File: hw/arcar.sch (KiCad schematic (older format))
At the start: 30 parts

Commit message: updated schematic, change microcontoler to ATmega328PB and added H bridge, MPU-6050, USB to UART converter and power source
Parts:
- removed C?: 1000u/50V, symbol CP
- removed D?: D, symbol D
- removed D?: D_Bridge_+-AA, symbol D_Bridge_+-AA
- removed J?: POWER, symbol Conn_01x02
- removed M? (x2): Motor_DC, symbol Motor_DC
- removed Q?: Q_NMOS_DGS, symbol Q_NMOS_DGS
- removed R?: 1k, symbol R
- removed U?: ATMEGA328P-AU, Housings_QFP:TQFP-32_7x7mm_Pitch0.8mm, symbol ATMEGA328P-AU
- added C1, C11, C2, C3, C4, C5, C6, C7: 100n, symbol C
- added C12: 2n2, symbol C
- added C13: 4700u/50V, symbol CP
- added C14: 470n, symbol C
- added C8: 10n, symbol C
- added J1: USB_B_Micro, Connectors:USB_Micro-B_10103594-0001LF, symbol USB_B_Micro
- added J2: HEADER, symbol Conn_01x10
- added J3: MOTOR, symbol Conn_01x02
- added R1: 10k, symbol R
- added R3, R4: 4k7, symbol R
- added U1: USBLC6-2SC6, TO_SOT_Packages_SMD:SOT-23-6, symbol USBLC6-2SC6
- added U2: ATMEGA328PB-AU, Housings_QFP:TQFP-32_7x7mm_Pitch0.8mm, symbol ATMEGA328PB-AU
- added U3: CP2102, Housings_DFN_QFN:QFN-28-1EP_5x5mm_Pitch0.5mm, symbol CP2102
- added U4: MPU-6050, symbol MPU-6050
- added U6: TLE52062GAUMA1, TO_SOT_Packages_SMD:TO-263-7_TabPin4, symbol TLE52062GAUMA1
- gave numbers to parts that had none: 21
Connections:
- net labels added: +5V, MOTOR_ERR, MOTOR_PWM1, MOTOR_PWM2, MPU-6050-INT, PD4, PD5, PD6, PD7, PE0, PE1, PE2, PE3
- net labels removed: MOTOR
- wire segments 85 -> 162
- no-connect marks 19 -> 23
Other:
- note removed: "BLOKOVÁNÍ"
- note removed: "ZDROJ"
- note removed: "zatím neznámích parametrů"
- note removed: "← MOŽNOSTI ↓"
- moved on the sheet: C10, C9, D1, D2, D3, D4, D5, P1, R2, R5, R6, R7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

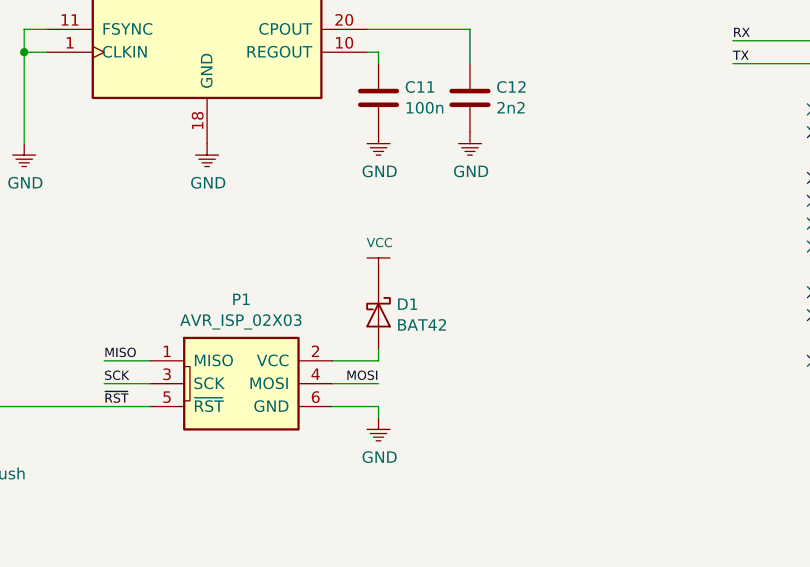
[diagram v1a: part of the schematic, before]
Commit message: updated schematic, chnde ISP VCC conection before LDO
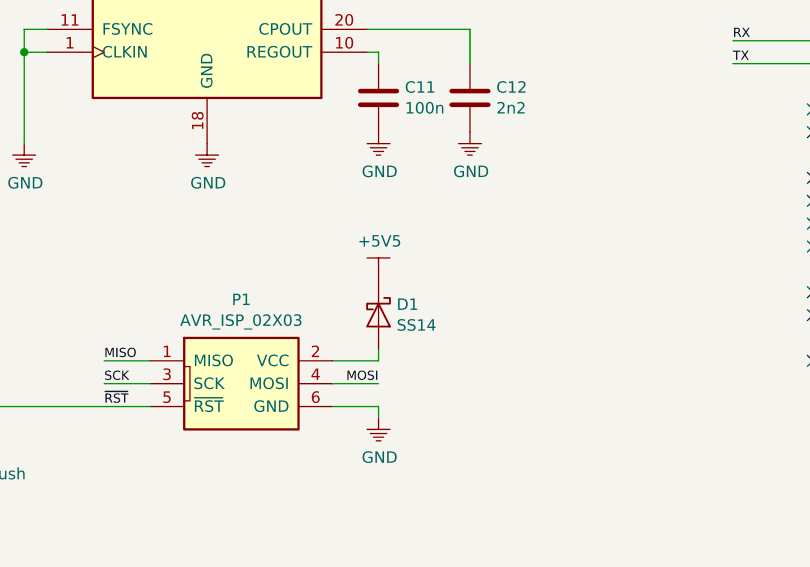
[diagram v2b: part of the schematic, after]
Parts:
- D1: value BAT42 -> SS14
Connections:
- net VCC: no longer D1.1 (K)
- new net +5V5: D1.1 (K)
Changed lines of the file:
@@
 P 7550 5600
 F 0 "D1" V 7504 5679 50  0000 L CNN
-F 1 "BAT42" V 7595 5679 50  0000 L CNN
+F 1 "SS14" V 7595 5679 50  0000 L CNN
 F 2 "" H 7550 5600 50  0001 C CNN
 F 3 "" H 7550 5600 50  0001 C CNN
 	1    7550 5600
 	0    1    1    0
-$EndComp
-$Comp
-L VCC #PWR021
-U 1 1 59F5914F
-P 7550 5450
-F 0 "#PWR021" H 7550 5300 50  0001 C CNN
-F 1 "VCC" H 7555 5616 40  0000 C CNN
-F 2 "" H 7550 5450 50  0001 C CNN
-F 3 "" H 7550 5450 50  0001 C CNN
-	1    7550 5450
-	1    0    0    -1
 $EndComp
 Text Label 9100 4200 0    40   ~ 0
@@
 Text Label 9900 1600 0    40   ~ 0
 PE3
+$Comp
+L +5V5 #PWR?
+U 1 1 59FB343D
+P 7550 5450
+F 0 "#PWR?" H 7550 5150 50  0001 C CNN
+F 1 "+5V5" H 7555 5623 50  0000 C CNN
+F 2 "" H 7550 5450 50  0001 C CNN
+F 3 "" H 7550 5450 50  0001 C CNN
+	1    7550 5450
+	1    0    0    -1
+$EndComp
 $EndSCHEMATC

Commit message: updated schematic
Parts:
- removed J2: HEADER, symbol Conn_01x10
- removed M1: screw, symbol screw
- removed U4: MPU-6050, symbol MPU-6050
- removed Y1: 8MHz, symbol Crystal
- added AFF1: LTS-6960HR, Displays_7-Segment:LTS-69xx, symbol LTS-6960HR
- added C13: 100n, symbol C
- added C14: 10u, symbol C
- added J2: GPIO, symbol Conn_01x04
- added R10, R11, R12, R6, R7, R8, R9: 330R, symbol R
- added R13, R5: 10k, symbol R
- added U4: ULN2003A, symbol ULN2003A
- added U5: LSM9DS1, Housings_LGA:LGA-24L_3x3.5mm_Pitch0.43mm, symbol LSM9DS1
- C10: value 18p -> 100n
- C12: value 2n2 -> 100n
- C9: value 18p -> 10n
- D1: value SS14 -> SK32SMA
- renumbered C13 to C15, C14 to C16, C7 to C6, C6 to C7, M2 to M1, M3 to M2, M4 to M3, R5 to R14, R6 to R15, R7 to R16, R8 to R17, U5 to U6, U6 to U7, U7 to U8
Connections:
- net +3V3: now also C11.2, C12.2, C13.2, C14.2, J2.3 (Pin_3), R13.1, R5.1, U5.1 (VDDIO), U5.22 (VDD), U5.23 (VDD), U5.3 (VDDIO), U5.7 (CS_A/G), U5.8 (CS_M)
- net GND: now also C10.2, C11.1, C12.1, C9.2, C13.1, C14.1, J2.4 (Pin_4), U4.8 (GND), U5.14 (RES), U5.15 (RES), U5.16 (RES), U5.17 (RES), U5.18 (RES), U5.19 (GND), U5.20 (GND); no longer C10.1, C11.2, C12.2, C9.1
- net MOTOR_ERR: now also U2.12 ((CLKO/ICP1/PTCXY)PB0); no longer U2.1 ((OC2B/INT1/PTCXY)PD3)
- net SCL: now also R4.2, U5.2 (SCL/SPC); no longer R3.2
- net SDA: now also R3.2, U5.4 (SDA/SDI/SDO); no longer R4.2
- net VCC: now also AFF1.3 (C.A.), AFF1.8 (C.A.), U4.9 (COM)
- net MPU-6050-INT renamed INT1_A/G
- net INT1_A/G: now also U5.11 (INT1_A/G)
- net PD4 renamed INT_M
- net INT_M: now also U5.10 (INT_M)
- net PD5 renamed SEG_C
- net SEG_C: now also U4.3 (I3)
- net PD6 renamed SEG_D
- net SEG_D: now also U4.4 (I4)
- net PD7 renamed SEG_E
- net SEG_E: now also U4.5 (I5)
- net PE0 renamed SEG_A
- net SEG_A: now also U4.1 (I1)
- net PE1 renamed SEG_B
- net SEG_B: now also U4.2 (I2)
- net PE2 renamed SEG_F
- net SEG_F: now also U4.6 (I6)
- net PE3 renamed SEG_G
- net SEG_G: now also U4.7 (I7)
- net XTAL1 renamed GPIO1
- net GPIO1: now also J2.1 (Pin_1); no longer C9.2
- net XTAL2 renamed GPIO2
- net GPIO2: now also J2.2 (Pin_2); no longer C10.2
- new net: C9.1, U5.21 (CAP)
- new net: C10.1, U5.24 (C1)
- new net: R5.2, U5.5 (SDO_A/G)
- new net: R13.2, U5.6 (SDO_M)
- new net: R12.2, U4.10 (O7)
- new net: R11.2, U4.11 (O6)
- new net: R10.2, U4.12 (O5)
- new net: R9.2, U4.13 (O4)
- new net: R8.2, U4.14 (O3)
- new net: R7.2, U4.15 (O2)
- new net: R6.2, U4.16 (O1)
- new net: AFF1.1 (e), R10.1
- new net: AFF1.10 (g), R12.1
- new net: AFF1.2 (d), R9.1
- new net: AFF1.4 (c), R8.1
- new net: AFF1.6 (b), R7.1
- new net: AFF1.7 (a), R6.1
- new net: AFF1.9 (f), R11.1
- new net INT2_A/G: U2.1 ((OC2B/INT1/PTCXY)PD3), U5.12 (INT2_A/G)
- no-connect marks 23 -> 21
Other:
- note added: "A"
- note added: "B"
- note added: "C"
- note added: "D"
- note added: "E"
- note added: "F"
- note added: "G"
- moved on the sheet: C15, C16, C2, C3, C4, C5, C6, C8, D1, D2, D3, D4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
